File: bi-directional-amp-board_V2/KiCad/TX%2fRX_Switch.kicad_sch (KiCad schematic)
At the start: 9 parts

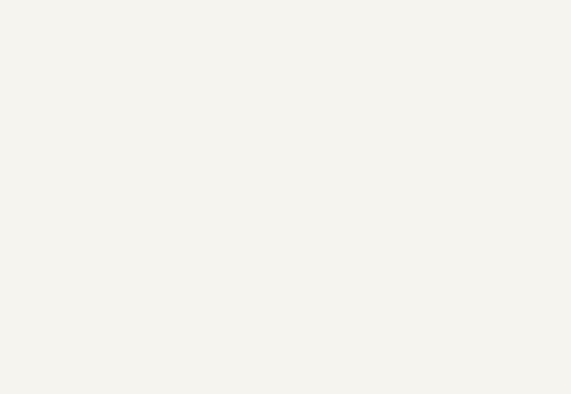
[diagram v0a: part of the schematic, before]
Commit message: re importing eagle files to kicad
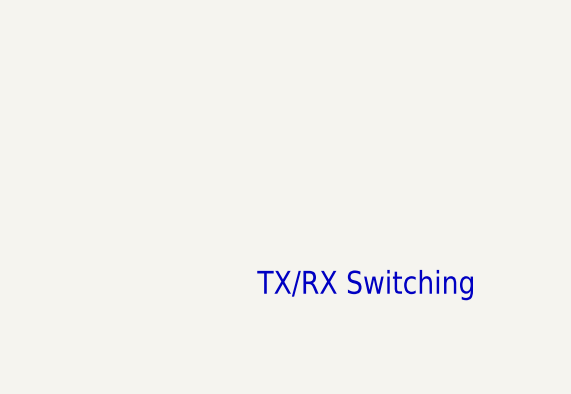
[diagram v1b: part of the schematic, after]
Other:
- note added: "TX/RX Switching"
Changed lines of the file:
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@@
 (kicad_sch (version 20211123) (generator eeschema)
-  (paper "User" 490.22 254.406)
+  (paper "A2")
   (junction (at 163.83 97.79) (diameter 0) (color 0 0 0 0)
   )
@@
     (effects (font (size 1.778 1.5113)) (justify left bottom))
   )
+  (text "TX/RX Switching" (at 212.09 205.74 180)
+    (effects (font (size 2.54 2.159)) (justify left bottom))
+  )
   (text "1%" (at 122.428 102.616 180)

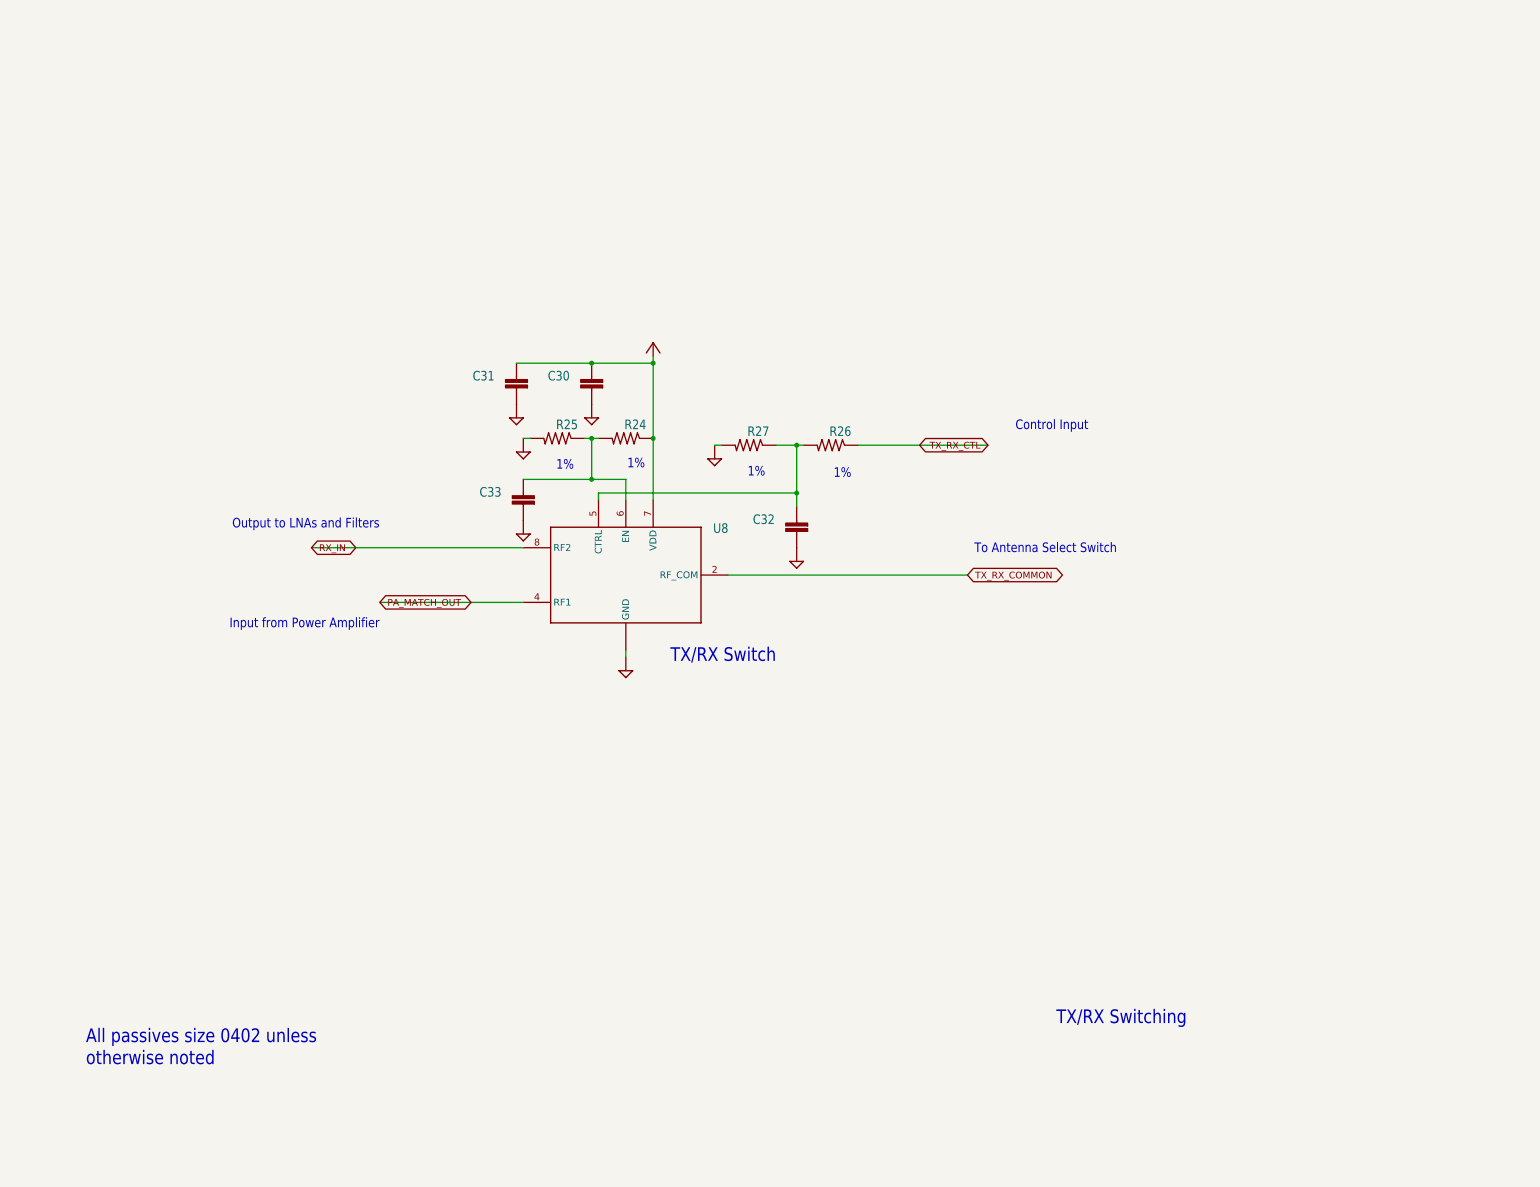
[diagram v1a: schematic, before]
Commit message: Updated KiCAD import of bidirectional amplifier. Still a bit broken, but better now.
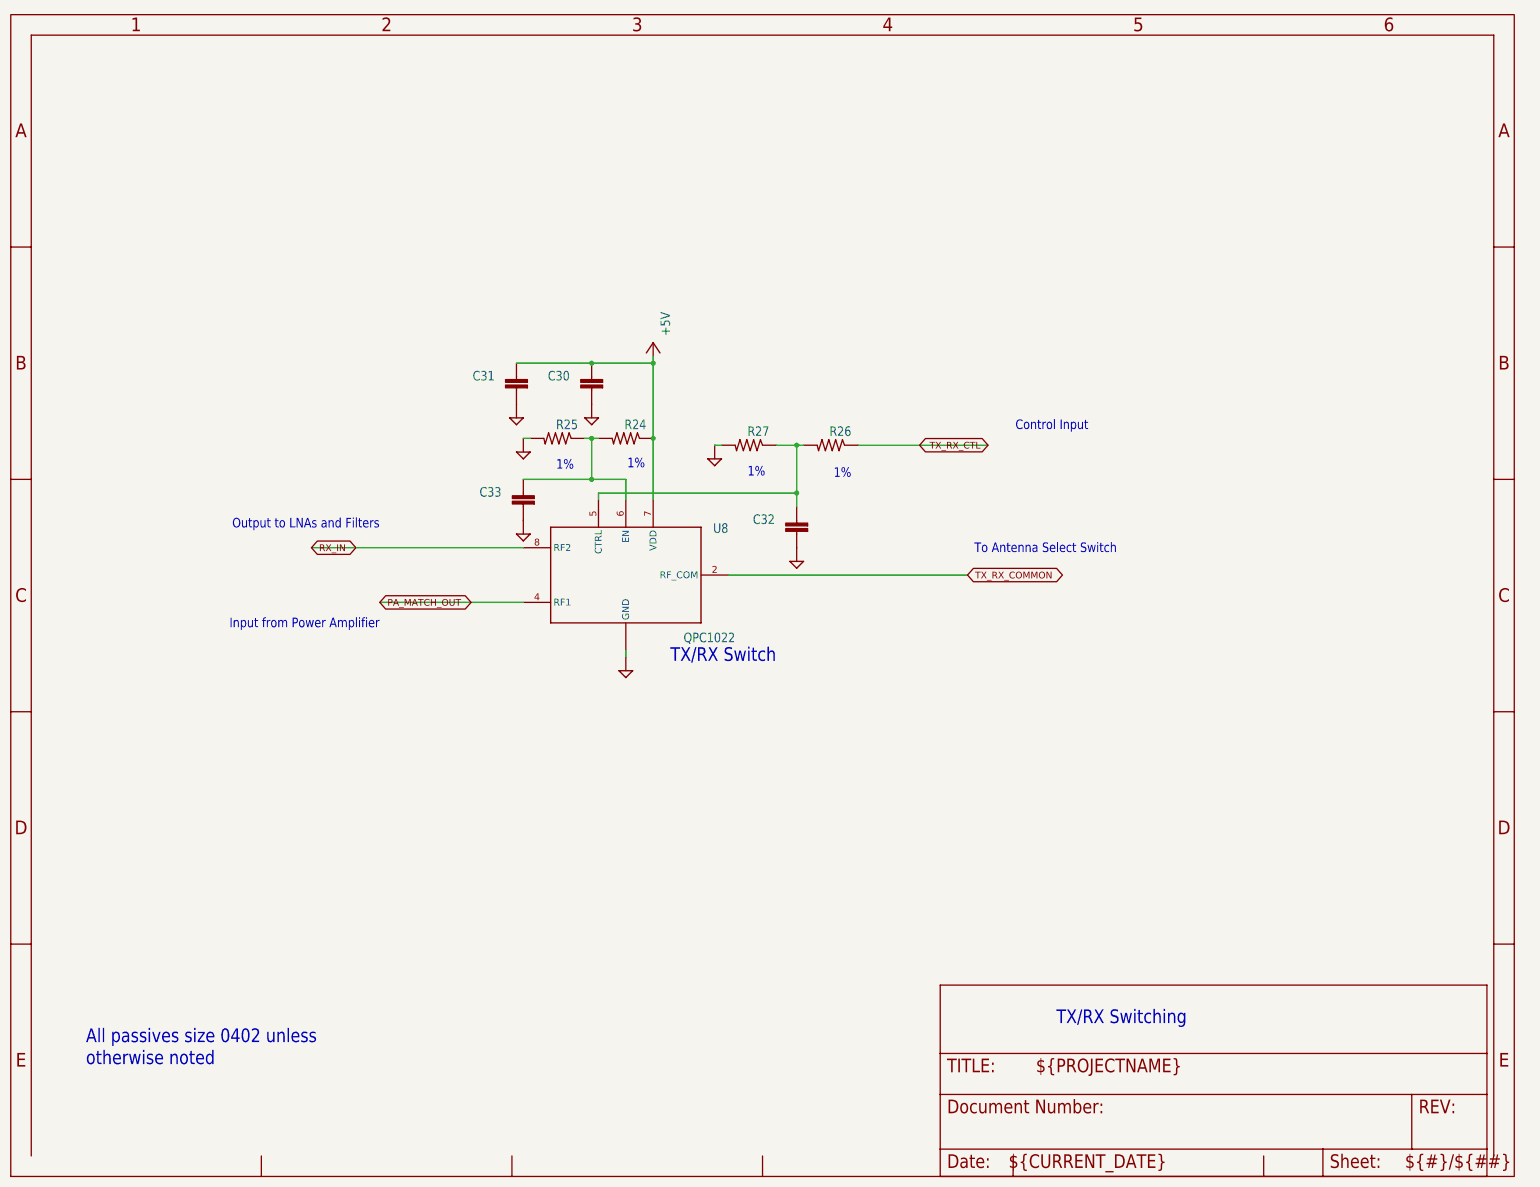
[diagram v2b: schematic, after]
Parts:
- C30, C33: value (none) -> C-EU0402-B-NOSILK; footprint (none) -> Bidirectional_Amp:.0402-B-NOSILK; MFR (none) -> Murata; MPN (none) -> GCM1555C1H101JA16D
- C31: value (none) -> C-EU0402-B-NOSILK; footprint (none) -> Bidirectional_Amp:.0402-B-NOSILK; MFR (none) -> TDK Corporation; MPN (none) -> CGA2B1X7R1C104K050BC
- C32: value (none) -> C-EU0402-B-NOSILK; footprint (none) -> Bidirectional_Amp:.0402-B-NOSILK
- R24, R26: value (none) -> R-US_0402-B-NOSILK; footprint (none) -> Bidirectional_Amp:.0402-B-NOSILK; MFR (none) -> Panasonic; MPN (none) -> ERJ-2RKF1002X
- R25, R27: value (none) -> R-US_0402-B-NOSILK; footprint (none) -> Bidirectional_Amp:.0402-B-NOSILK; MFR (none) -> Panasonic; MPN (none) -> ERJ-2RKF5621X
- U8: value (none) -> QPC1022; footprint (none) -> Bidirectional_Amp:QPC1022
